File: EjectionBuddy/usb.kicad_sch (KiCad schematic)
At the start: 4 parts, among them J1 USB_C_Receptacle_USB2.0_14P

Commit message: Finished! QR and instruction pending
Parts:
- removed R1, R2: 5.1k, Resistor_SMD:R_0603_1608Metric, symbol Device:R
- added R19, R20: 5.1k, Resistor_SMD:R_0603_1608Metric, symbol Device:R
- renumbered D1 to D10, J1 to J15
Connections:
- net D+: now also D10.2 (I/O1); no longer D10.3 (I/O2)
- net D-: now also D10.3 (I/O2); no longer D10.2 (I/O1)
- net GND: now also R19.2, R20.2
- net CC1: now reaches J15.A5 (CC1)
- net CC1: now also R19.1
- net CC2: now reaches J15.B5 (CC2)
- net CC2: now also R20.1

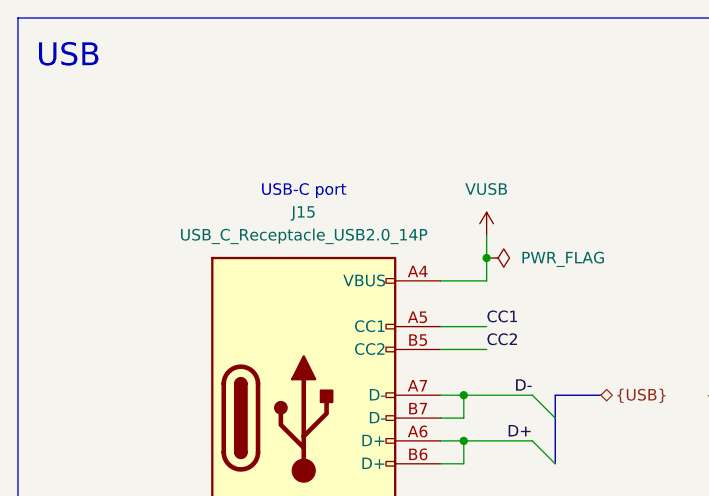
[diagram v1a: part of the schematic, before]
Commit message: Side-mcu stm -> attiny, with improvements here and there
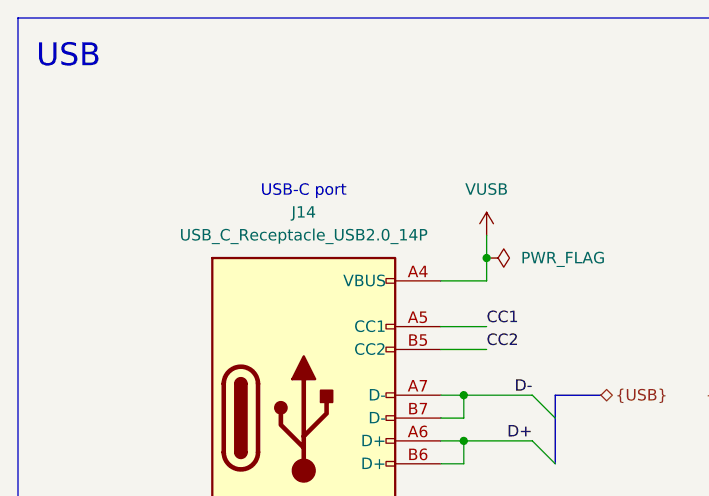
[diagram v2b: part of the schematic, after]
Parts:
- renumbered J15 to J14
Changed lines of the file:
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@@
 		(on_board yes)
 		(dnp no)
-		(property "Reference" "#PWR0102"
+		(property "Reference" "#PWR0101"
 			(at 127 83.82 0)
 			(effects
@@
 			(project "EjectionBuddy"
 				(path "/8eb0a75f-d01a-4f77-b089-39fac6868a70/3a53a976-0a1f-4550-b46f-9acfd9ed9642"
-					(reference "#PWR0102")
+					(reference "#PWR0101")
 					(unit 1)
 				)
@@
 		(on_board yes)
 		(dnp no)
-		(property "Reference" "#FLG010"
+		(property "Reference" "#FLG011"
 			(at 69.215 41.91 0)
 			(effects
@@
 			(project "EjectionBuddy"
 				(path "/8eb0a75f-d01a-4f77-b089-39fac6868a70/3a53a976-0a1f-4550-b46f-9acfd9ed9642"
-					(reference "#FLG010")
+					(reference "#FLG011")
 					(unit 1)
 				)
@@
 		(dnp no)
 		(fields_autoplaced yes)
-		(property "Reference" "J15"
+		(property "Reference" "J14"
 			(at 46.99 36.83 0)
 			(effects
@@
 			(project "EjectionBuddy"
 				(path "/8eb0a75f-d01a-4f77-b089-39fac6868a70/3a53a976-0a1f-4550-b46f-9acfd9ed9642"
-					(reference "J15")
+					(reference "J14")
 					(unit 1)
 				)
@@
 		(on_board yes)
 		(dnp no)
-		(property "Reference" "#PWR0103"
+		(property "Reference" "#PWR0102"
 			(at 46.99 93.98 0)
 			(effects
@@
 			(project "EjectionBuddy"
 				(path "/8eb0a75f-d01a-4f77-b089-39fac6868a70/3a53a976-0a1f-4550-b46f-9acfd9ed9642"
-					(reference "#PWR0103")
+					(reference "#PWR0102")
 					(unit 1)
 				)
@@
 		(dnp no)
 		(fields_autoplaced yes)
-		(property "Reference" "#PWR0101"
+		(property "Reference" "#PWR0100"
 			(at 127 50.8 0)
 			(effects
@@
 			(project "EjectionBuddy"
 				(path "/8eb0a75f-d01a-4f77-b089-39fac6868a70/3a53a976-0a1f-4550-b46f-9acfd9ed9642"
-					(reference "#PWR0101")
+					(reference "#PWR0100")
 					(unit 1)
 				)
@@
 		(on_board yes)
 		(dnp no)
-		(property "Reference" "#PWR0104"
+		(property "Reference" "#PWR0103"
 			(at 81.28 93.98 0)
 			(effects
@@
 			(project "EjectionBuddy"
 				(path "/8eb0a75f-d01a-4f77-b089-39fac6868a70/3a53a976-0a1f-4550-b46f-9acfd9ed9642"
-					(reference "#PWR0104")
+					(reference "#PWR0103")
 					(unit 1)
 				)
@@
 		(on_board yes)
 		(dnp no)
-		(property "Reference" "#PWR0105"
+		(property "Reference" "#PWR0104"
 			(at 96.52 93.98 0)
 			(effects
@@
 			(project "EjectionBuddy"
 				(path "/8eb0a75f-d01a-4f77-b089-39fac6868a70/3a53a976-0a1f-4550-b46f-9acfd9ed9642"
-					(reference "#PWR0105")
+					(reference "#PWR0104")
 					(unit 1)
 				)
@@
 		(dnp no)
 		(fields_autoplaced yes)
-		(property "Reference" "#PWR0100"
+		(property "Reference" "#PWR099"
 			(at 67.31 43.18 0)
 			(effects
@@
 			(project "EjectionBuddy"
 				(path "/8eb0a75f-d01a-4f77-b089-39fac6868a70/3a53a976-0a1f-4550-b46f-9acfd9ed9642"
-					(reference "#PWR0100")
-					(unit 1)
-				)
+					(reference "#PWR099")
+					(unit 1)
+				)
